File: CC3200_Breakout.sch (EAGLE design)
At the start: 51 parts, among them J22 M10X2, J23 M10X2, U15 AT25FS010, Y2 32.768KHz, Y3 407MHz

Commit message: proper files added now, ready to finish routing
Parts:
- added C1, C11, C13, C14, C16, C17, C19, C21, C22, C5, C51, C9: 0.1uF, SparkFun-Capacitors:0.1UF-0402-16V-10%
- added C10, C12, C2, C20, C6: 1.0uF, SparkFun-Capacitors:1.0UF-0402-16V-10%
- added C15, C18: 4.7nF, SparkFun-Retired:4.7NF-50V-10%(0603)
- added C3, C4, C7: 10uF, SparkFun-Capacitors:10UF-0603-6.3V-20%
- added C46, C49: 47uF, SparkFun-Capacitors:0.1UF-0603-25V-5%
- added C52: 100uF, SparkFun-Capacitors:100UF-POLAR-25V-20%(ELEC)
- added C53: 0.1uF, resistor:C-USC0402K
- added D1: 1A/30V, diode:SCHOTTKY-DIODESMD
- added FB1, FB2: 40Ω/1.5A, SparkFun-Coils:FERRITE_BEAD-0603
- added J1: MJ-3536N, con-cuistack:MJ-3536N
- added J2: (no value), SparkFun-Connectors:USB_MICRO-B_SMT
- added J3, J4: SJ-3515-SMT, con-cuistack:SJ-3515-SMT
- added JMP1, JMP2, JMP3, JMP4, JMP5: 0R-JUMPA, jump-0r-smd:0R-JUMPA
- added JP1: (no value), SparkFun-Retired:JUMPER-2PTH
- added R2, R5, R7: 10k, SparkFun-Resistors:10KOHM-0603-1/10W-1%
- added R3, R4: 1k, SparkFun-Resistors:1KOHM-0603-1/10W-1%
- added TERMINAL_BLOCK: (no value), SparkFun-Connectors:CONN_04JST-PTH
- added TP1, TP13, TP2, TP3: (no value), SparkFun-Connectors:CONN_01
- added U1: TLV320AIC3254_RHB_32, TLV320AIC3254:TLV320AIC3254_RHB_32
- added U2: TPA2012D2_RTJ_20, TPA2012D2_RTJ_20:TPA2012D2_RTJ_20
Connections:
- removed net 50: J22.20, U$1.GPIO_00
- removed net 53: J22.16, U$1.GPIO_30
- removed net 61: J22.9, U$1.GPIO_06
- removed net 63: J22.14, U$1.GPIO_08
- removed net 64: J22.18, U$1.GPIO_09
- removed net N$91: J23.10
- new net +3V3: C5.1, C6.1, U1.LDOIN
- new net AA_LOL: R4.2, U1.LOL
- new net AA_LOR: R3.2, U1.LOR
- new net BCLK_IN: JMP3-0R.2, TP13.1, U1.BCLK, U1.MCLK
- new net BCLK_J3: J22.16, JMP3-0R.1, U$1.GPIO_30
- new net CODEC_RESET: J22.9, JMP1-0R.3, U$1.GPIO_06
- new net DIN: JMP4-0R.1, JMP5-0R.3, U1.DIN/MFP1
- new net DIN_J3: J22.18, JMP4-0R.2, U$1.GPIO_09
- new net DOUT: JMP4-0R.3, JMP5-0R.1, U1.DOUT/MFP2
- new net DOUT_J3: J22.20, JMP5-0R.2, U$1.GPIO_00
- new net FSYNC_IN: JMP2-0R.2, U1.WCLK
- new net FSYNC_J3: J22.14, JMP2-0R.1, U$1.GPIO_08
- new net LOUT1: TERMINAL_BLOCK.4, U2.OUTL+
- new net LOUT2: TERMINAL_BLOCK.3, U2.OUTL-
- new net MASTER_RESET: C53.1, J23.10, JMP1-0R.1, R7.1
- new net MICBIAS: R5.2, U1.MICBIAS
- new net N$23: TP2.1, U1.MISO/MFP4
- new net N$25: C3.1, U1.REF
- new net N$26: TP1.1, U1.SCLK/MFP3
- new net N$34: TP3.1, U1.GPIO/MFP5
- new net N$35: JP1.2, R2.2, U2.G1
- new net N$37: C7.1, U1.DVDD
- new net N$38: C22.2, J4.T, J4.TS
- new net N$39: C14.2, U2.INL+
- new net N$41: C13.1, C15.1, R3.1
- new net N$42: C13.2, U2.INL-
- new net N$43: C16.2, U2.INR-
- new net N$44: C16.1, C18.1, R4.1
- new net N$45: C17.2, U2.INR+
- new net N$46: C21.2, J4.R, J4.RS
- new net N$55: C46.2, J3.R, J3.RS
- new net N$56: C49.2, J3.T, J3.TS
- new net N$57: C51.2, J1.T, J1.TS, R5.1
- new net N$58: D1.A, FB2.2
- new net N$59: FB2.1, J2.VBUS
- new net N$60: FB1.2, J2.GND
- new net RESET_OUT: JMP1-0R.2, U1.RESET
- new net ROUT1: TERMINAL_BLOCK.2, U2.OUTR+
- new net ROUT2: TERMINAL_BLOCK.1, U2.OUTR-
- new net SJ_HPL: C49.1, U1.HPL
- new net SJ_HPR: C46.1, U1.HPR
- new net SJ_IN1L: C21.1, U1.IN1_L
- new net SJ_IN1R: C22.1, U1.IN1_R
- new net SJ_IN2L: U1.IN2_L
- new net SJ_IN2R: C51.1, U1.IN2_R
- new net SJ_IN3L: U1.IN3_L
- new net SJ_IN3R: U1.IN3_R
- new net VCCA: C4.1, U1.AVDD, U2.*SDL, U2.*SDR
- new net VCC_5V_MCU: D1.C
- new net VCC_BRD1: C1.1, C10.1, C11.1, C12.1, C19.1, C2.1, C20.1, C52.+, C9.1, JP1.1, U1.LDO_SELECT, U1.OVIDD, U2.AVDD, U2.PVDD, U2.PVDD_2
- net 3.3V: now also R7.2
- net GND: now also C1.2, C10.2, C11.2, C12.2, C14.1, C15.2, C17.1, C18.2, C19.2, C2.2, C20.2, C3.2, C4.2, C5.2, C52.-, C53.2, C6.2, C7.2, C9.2, FB1.1, J1.S, J2.SHIELD, J3.S, J4.S, R2.1, U1.AVSS, U1.DVSS, U1.EPAD, U1.OVISS, U1.SPI_SELECT, U2.AGND, U2.EPAD, U2.G0, U2.PGND, U2.PGND_2
- net SCL: now also U1.SCL/SSZ
- net SDA: now also U1.SDA/MOSI

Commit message: routed
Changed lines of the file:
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@@
 <part name="C1" library="SparkFun-Capacitors" deviceset="0.1UF" device="-0402-16V-10%" value="0.1uF"/>
 <part name="C2" library="SparkFun-Capacitors" deviceset="1.0UF" device="-0402-16V-10%" value="1.0uF"/>
-<part name="GND33" library="SparkFun-PowerSymbols" deviceset="GND" device=""/>
-<part name="GND34" library="SparkFun-PowerSymbols" deviceset="GND" device=""/>
 <part name="GND35" library="SparkFun-PowerSymbols" deviceset="GND" device=""/>
 <part name="TP1" library="SparkFun-Connectors" deviceset="CONN_01" device=""/>
 <part name="TP2" library="SparkFun-Connectors" deviceset="CONN_01" device=""/>
-<part name="GND36" library="SparkFun-PowerSymbols" deviceset="GND" device=""/>
 <part name="GND37" library="SparkFun-PowerSymbols" deviceset="GND" device=""/>
 <part name="C3" library="SparkFun-Capacitors" deviceset="10UF" device="-0603-6.3V-20%" value="10uF"/>
@@
 <part name="R7" library="SparkFun-Resistors" deviceset="10KOHM" device="-0603-1/10W-1%" value="10k"/>
 <part name="SUPPLY7" library="SparkFun-Aesthetics" deviceset="3.3V" device=""/>
+<part name="GND64" library="SparkFun-Aesthetics" deviceset="GND" device=""/>
+<part name="GND33" library="SparkFun-Aesthetics" deviceset="GND" device=""/>
+<part name="GND34" library="SparkFun-Aesthetics" deviceset="GND" device=""/>
 </parts>
 <sheets>
@@
 <instance part="C1" gate="G$1" x="-114.3" y="149.86"/>
 <instance part="C2" gate="G$1" x="-127" y="149.86"/>
-<instance part="GND33" gate="1" x="-127" y="144.78"/>
-<instance part="GND34" gate="1" x="-114.3" y="144.78"/>
 <instance part="GND35" gate="1" x="-83.82" y="129.54"/>
 <instance part="TP1" gate="G$1" x="-76.2" y="127"/>
 <instance part="TP2" gate="G$1" x="-76.2" y="119.38"/>
-<instance part="GND36" gate="1" x="-66.04" y="106.68"/>
 <instance part="GND37" gate="1" x="35.56" y="104.14"/>
 <instance part="C3" gate="G$1" x="45.72" y="106.68"/>
@@
 <instance part="JMP1" gate="-0R" x="203.2" y="68.58"/>
 <instance part="JMP1" gate="G$2" x="200.66" y="71.12"/>
+<instance part="GND64" gate="1" x="-66.04" y="106.68"/>
+<instance part="GND33" gate="1" x="-114.3" y="144.78"/>
+<instance part="GND34" gate="1" x="-127" y="144.78"/>
 </instances>
 <busses>
@@
 <net name="GND" class="0">
 <segment>
-<pinref part="C2" gate="G$1" pin="2"/>
-<pinref part="GND33" gate="1" pin="GND"/>
-</segment>
-<segment>
-<pinref part="C1" gate="G$1" pin="2"/>
-<pinref part="GND34" gate="1" pin="GND"/>
-</segment>
-<segment>
 <pinref part="U1" gate="A" pin="OVISS"/>
 <wire x1="-50.8" y1="134.62" x2="-83.82" y2="134.62" width="0.1524" layer="91"/>
 <pinref part="GND35" gate="1" pin="GND"/>
 <wire x1="-83.82" y1="134.62" x2="-83.82" y2="132.08" width="0.1524" layer="91"/>
-</segment>
-<segment>
-<pinref part="GND36" gate="1" pin="GND"/>
-<wire x1="-66.04" y1="109.22" x2="-66.04" y2="121.92" width="0.1524" layer="91"/>
-<pinref part="U1" gate="A" pin="SPI_SELECT"/>
-<wire x1="-66.04" y1="121.92" x2="-50.8" y2="121.92" width="0.1524" layer="91"/>
 </segment>
 <segment>
@@
 <pinref part="GND62" gate="1" pin="GND"/>
 </segment>
-</net>
+<segment>
+<wire x1="-66.04" y1="109.22" x2="-66.04" y2="121.92" width="0.1524" layer="91"/>
+<pinref part="U1" gate="A" pin="SPI_SELECT"/>
+<wire x1="-66.04" y1="121.92" x2="-50.8" y2="121.92" width="0.1524" layer="91"/>
+<pinref part="GND64" gate="1" pin="GND"/>
+</segment>
+<segment>
+<pinref part="C1" gate="G$1" pin="2"/>
+<pinref part="GND33" gate="1" pin="GND"/>
+</segment>
+<segment>
+<pinref part="C2" gate="G$1" pin="2"/>
+<pinref part="GND34" gate="1" pin="GND"/>
+</segment>
+</net>

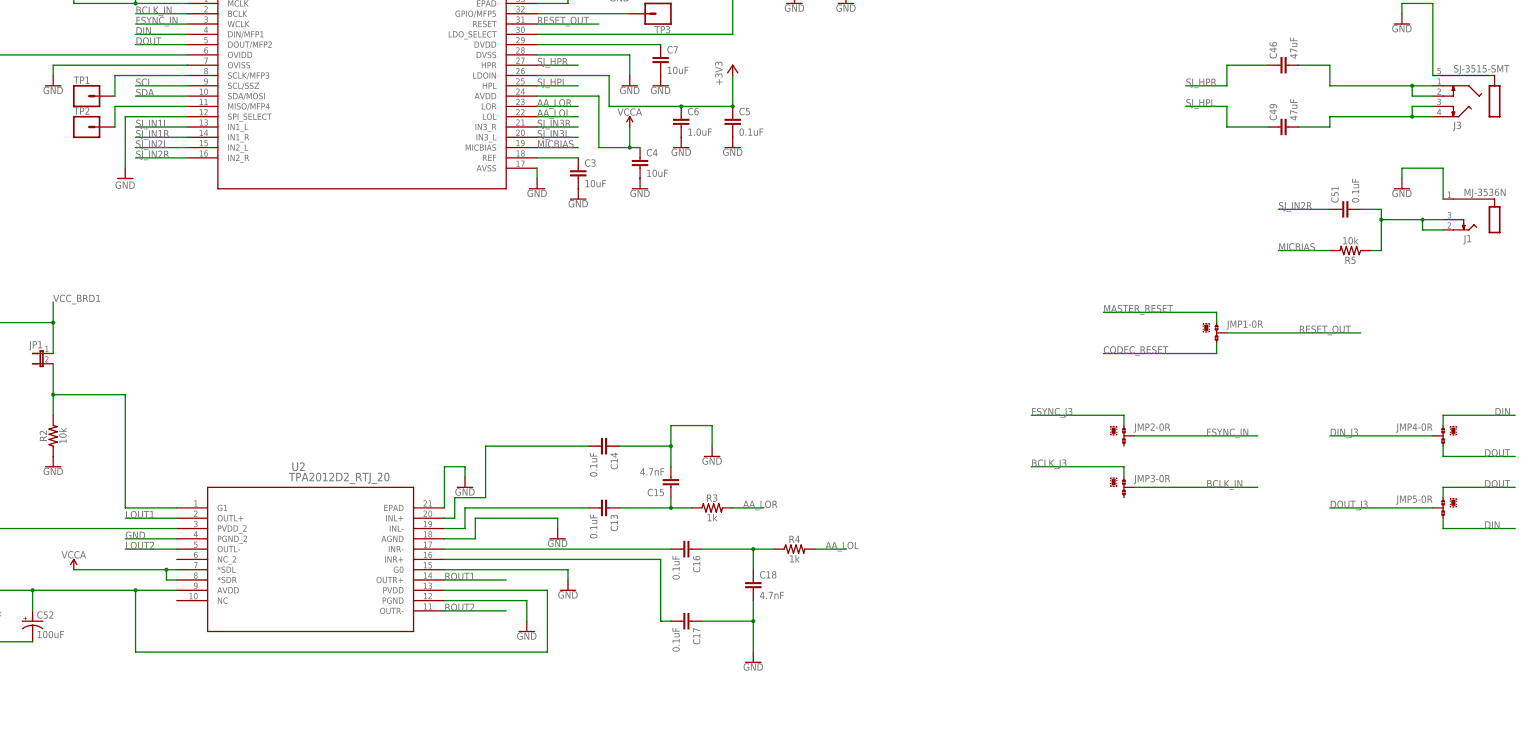
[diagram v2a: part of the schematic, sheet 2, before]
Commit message: Finished routing and reduced to 2 layers.
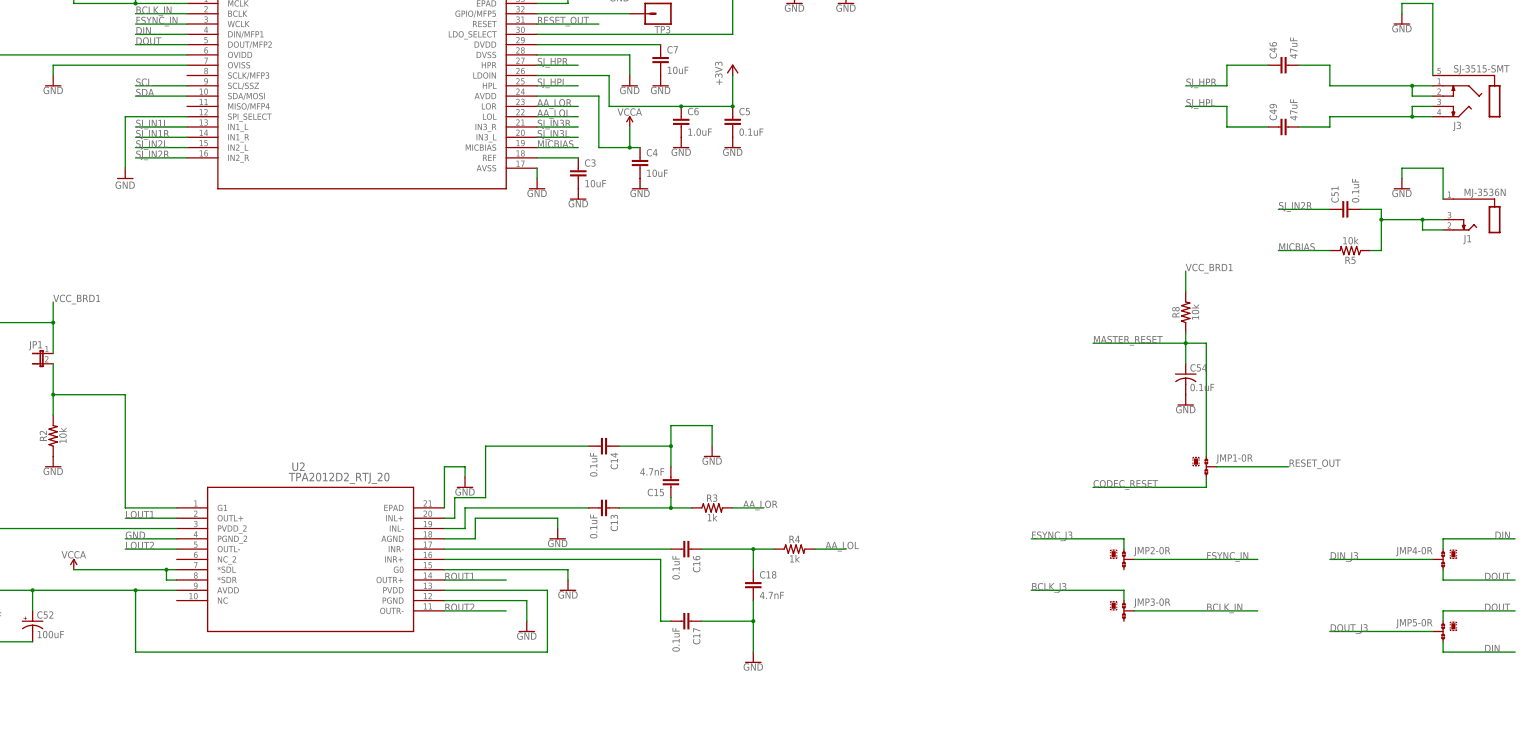
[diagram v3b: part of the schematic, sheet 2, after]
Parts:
- removed C53: 0.1uF, resistor:C-USC0402K
- removed J22, J23: M10X2, SparkFun-Connectors:M10X2
- removed JP90: M02LOCK, SparkFun-Connectors:M02LOCK
- removed R7: 10k, SparkFun-Resistors:10KOHM-0603-1/10W-1%
- removed TP1, TP2: (no value), SparkFun-Connectors:CONN_01
- added C54: 0.1uF, resistor:C-USC0402K
- added R8: 10k, SparkFun-Resistors:10KOHM-0603-1/10W-1%
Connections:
- removed net 16: J23.17
- removed net 17: J23.19
- removed net 21: J23.16
- removed net N$23: TP2.1, U1.MISO/MFP4
- removed net N$26: TP1.1, U1.SCLK/MFP3
- removed net N$47: J23.1
- removed net N$48: J23.3
- removed net N$49: J23.5
- removed net N$50: J23.7
- removed net N$51: J23.9
- removed net N$52: J23.11
- removed net N$53: J23.13
- removed net N$54: J23.15
- removed net N$81: J22.10
- removed net N$82: J22.12
- removed net VCC_BRD: J22.1
- removed net VCC_MCU_5V: J22.2
- net 15: no longer J23.20
- net 18: no longer J23.4
- net 3: no longer J22.7
- net 3.3V: no longer R7.2
- net 4: no longer J22.5
- net 45: no longer J23.8
- net 55: no longer J23.18
- net 57: no longer J22.6
- net 58: no longer J22.3
- net 59: no longer J22.11
- net 60: no longer J22.8
- net 62: no longer J22.15
- net BCLK_J3: no longer J22.16
- net CODEC_RESET: no longer J22.9
- net DIN_J3: no longer J22.18
- net DOUT_J3: no longer J22.20
- net FSYNC_J3: no longer J22.14
- net GND: now also C54.2; no longer C53.2, J22.4, J23.2
- net JTAG_TCK: no longer JP90.1
- net MASTER_RESET: now also C54.1, R8.1; no longer C53.1, J23.10, R7.1
- net N$22: no longer JP90.2
- net SCL: no longer J22.17
- net SDA: no longer J22.19
- net SPI_CLK: no longer J22.13
- net SPI_CS: no longer J23.6
- net SPI_MISO: no longer J23.14
- net SPI_MOSI: no longer J23.12
- net VCC_BRD1: now also R8.2
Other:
- moved on the sheet: JMP1-0R, JMP2-0R, JMP3-0R, JMP4-0R, JMP5-0R

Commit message: I get by with a little help from Artur
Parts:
- removed D1: 1A/30V, diode:SCHOTTKY-DIODESMD
- removed FB1, FB2: 40Ω/1.5A, SparkFun-Coils:FERRITE_BEAD-0603
- removed J2: (no value), SparkFun-Connectors:USB_MICRO-B_SMT
- added C53, C55: 10uF, rcl:C-USC1206
- added IC1: REG1117, burr-brown:REG1117
- added J5: POWER_JACK, SparkFun-Connectors:POWER_JACK
- added TP1, TP2, TP4: (no value), SparkFun-Connectors:CONN_01
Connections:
- removed net GND: C1.2, C10.2, C11.2, C12.2, C14.1, C15.2, C17.1, C18.2, C19.2, C2.2, C20.2, C23.2, C24.2, C25.2, C26.2, C27.2, C28.2, C29.2, C3.2, C30.2, C31.2, C32.2, C33.2, C34.2, C35.2, C36.2, C37.2, C38.2, C39.2, C4.2, C40.2, C41.2, C42.2, C43.2, C44.2, C45.2, C47.2, C48.2, C5.2, C50.1, C50.2, C52.-, C54.2, C6.2, C7.2, C8.2, C9.2, FB1.1, FL1.GND@1, FL1.GND@2, J1.S, J2.SHIELD, J3.S, J4.S, JP91.1, JTAG.2, L1.2, R2.1, R58.1, R59.1, R61.1, U$1.GND_TAB, U$3.SIGNAL, U1.AVSS, U1.DVSS, U1.EPAD, U1.OVISS, U1.SPI_SELECT, U15.GND, U2.AGND, U2.EPAD, U2.G0, U2.PGND, U2.PGND_2
- removed net N$58: D1.A, FB2.2
- removed net N$59: FB2.1, J2.VBUS
- removed net N$60: FB1.2, J2.GND
- removed net VCC_5V_MCU: D1.C
- new net SS: C1.2, C10.2, C11.2, C12.2, C14.1, C15.2, C17.1, C18.2, C19.2, C2.2, C20.2, C23.2, C24.2, C25.2, C26.2, C27.2, C28.2, C29.2, C3.2, C30.2, C31.2, C32.2, C33.2, C34.2, C35.2, C36.2, C37.2, C38.2, C39.2, C4.2, C40.2, C41.2, C42.2, C43.2, C44.2, C45.2, C47.2, C48.2, C5.2, C50.1, C52.-, C53.2, C54.2, C55.2, C6.2, C7.2, C8.2, C9.2, FL1.GND@1, FL1.GND@2, IC1.GND, J1.S, J3.S, J4.S, J5.GND, J5.GNDBREAK, JP91.1, JTAG.2, L1.2, R2.1, R58.1, R59.1, R61.1, U$1.GND_TAB, U$3.SIGNAL, U1.AVSS, U1.DVSS, U1.EPAD, U1.OVISS, U1.SPI_SELECT, U15.GND, U2.AGND, U2.EPAD, U2.G0, U2.PGND, U2.PGND_2
- new net V_IN: C55.1, IC1.VIN, J5.PWR
- net 58: now also TP1.1
- net 59: now also TP2.1
- net 60: now also TP4.1
- net V_BATT: now also C53.1, IC1.VOUT
